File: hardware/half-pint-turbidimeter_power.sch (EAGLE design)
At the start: 17 parts, among them U1 MCP73831

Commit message: minor edits to eagle schematics
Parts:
- removed D11: RED, SparkFun:LED0603
- removed JP2: STAND-OFF, SparkFun:STAND-OFF
- removed R2K: 2K, SparkFun:RESISTOR0402-RES
- removed R330: 330, SparkFun:RESISTOR0402-RES
- added D2: GREEN, SparkFun:LED0603
- added FRAME1: FRAME-LETTER, SparkFun-Aesthetics:FRAME-LETTER
- added R2: R330, SparkFun:RESISTOR0402-RES
- added R3: R2K, SparkFun:RESISTOR0402-RES
- D1: value GREEN -> RED
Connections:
- net GND: now also D2.C, R3.2; no longer D1.C, R2K.2
- net N$2: now also D2.A, R2.2; no longer D1.A, R1.2
- net N$3: now also D1.A, R1.1; no longer D11.A, R330.1
- net PROG: now also R3.1; no longer R2K.1
- net STAT: now also D1.C, R2.1; no longer D11.C, R1.1
- net VIN: now also R1.2; no longer R330.2
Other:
- note added: "AWQUA"
- note removed: "0.1""
- note removed: "Connection to 3.7V System"
- note removed: "N. Seidle"
- note removed: "Set for 500mA charging"
- moved on the sheet: +OUT-, 1UF, 2.2UF, D1, OPT_10NF, R1

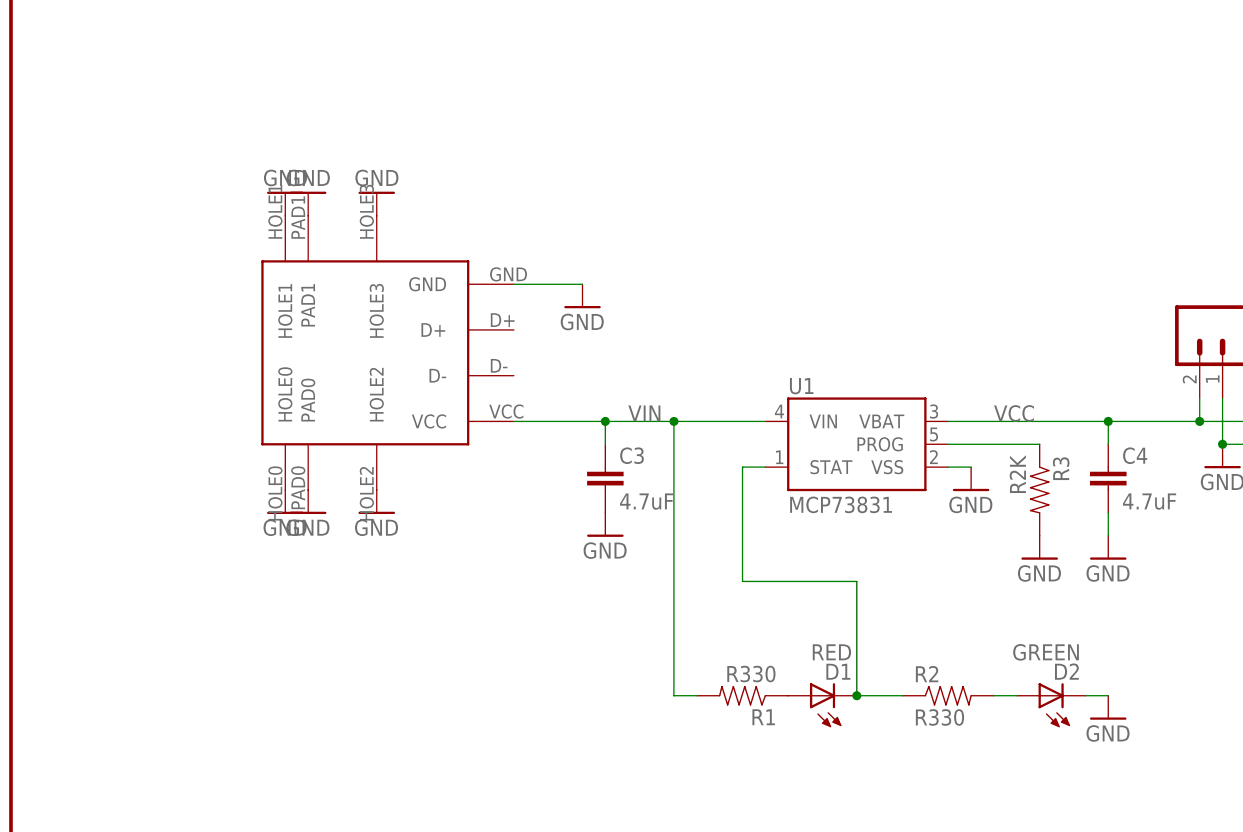
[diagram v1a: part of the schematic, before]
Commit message: added voltage protection diode
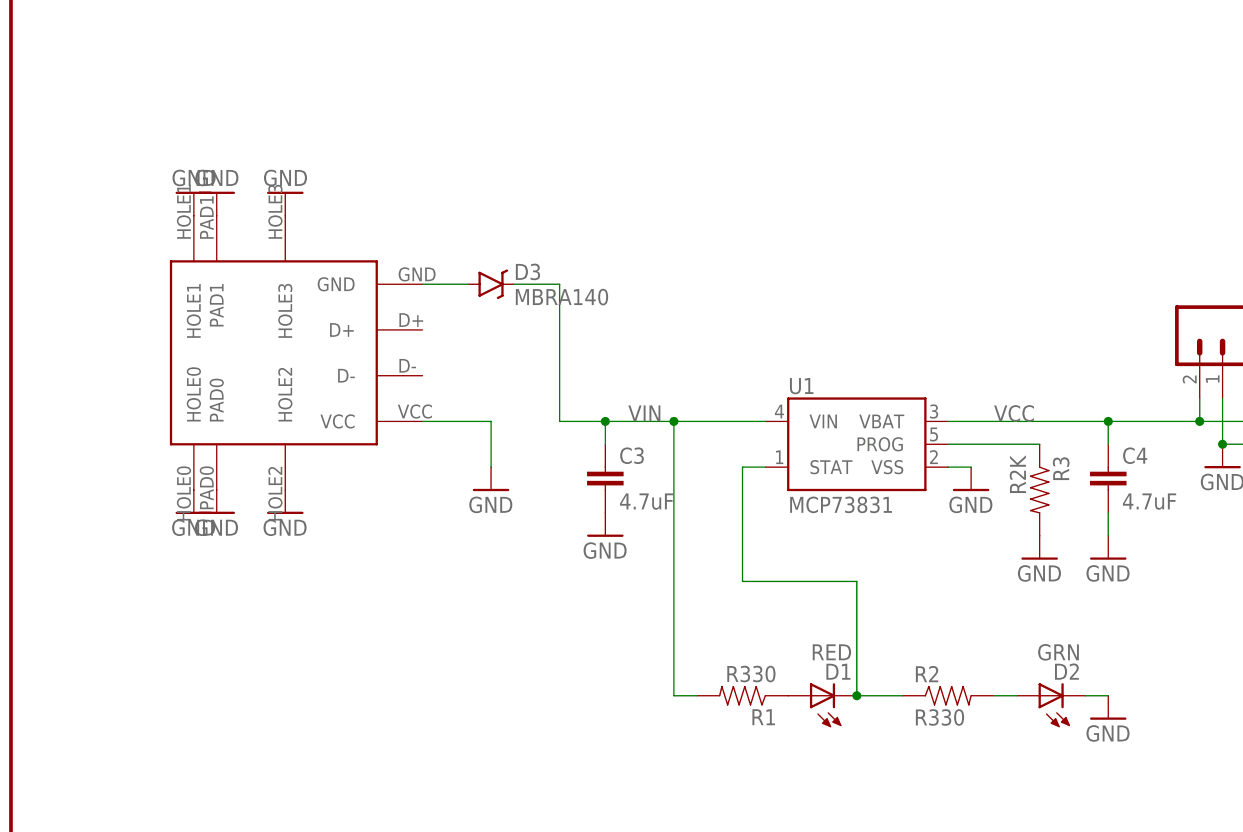
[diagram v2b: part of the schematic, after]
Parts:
- added D3: MBRA140, SparkFun-DiscreteSemi:MBRA140
- D2: value GREEN -> GRN
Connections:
- new net N$5: D3.A, U$3.GND
- net GND: now also U$3.VCC; no longer U$3.GND
- net VIN: now also D3.C; no longer U$3.VCC
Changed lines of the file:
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@@
 <part name="2.2UF" library="SparkFun-Passives" deviceset="CAP" device="0603-CAP"/>
 <part name="R2" library="SparkFun" deviceset="RESISTOR" device="0402-RES" value="R330"/>
-<part name="D2" library="SparkFun" deviceset="LED" device="0603" value="GREEN"/>
+<part name="D2" library="SparkFun" deviceset="LED" device="0603" value="GRN"/>
 <part name="GND3" library="SparkFun" deviceset="GND" device=""/>
 <part name="U$3" library="awqua_eagle_library" deviceset="USBMICRO-DX4R005JJ2" device=""/>
@@
 <part name="GND9" library="SparkFun" deviceset="GND" device=""/>
 <part name="FRAME1" library="SparkFun-Aesthetics" deviceset="FRAME-LETTER" device=""/>
+<part name="D3" library="SparkFun-DiscreteSemi" deviceset="MBRA140" device=""/>
 </parts>
 <sheets>
@@
 <instance part="D1" gate="G$1" x="111.76" y="88.9" rot="R90"/>
 <instance part="R1" gate="G$1" x="104.14" y="88.9" rot="R180"/>
-<instance part="GND15" gate="1" x="86.36" y="132.08"/>
+<instance part="GND15" gate="1" x="76.2" y="111.76"/>
 <instance part="GND14" gate="1" x="144.78" y="104.14"/>
 <instance part="GND17" gate="1" x="88.9" y="106.68"/>
@@
 <instance part="D2" gate="G$1" x="137.16" y="88.9" rot="R90"/>
 <instance part="GND3" gate="1" x="144.78" y="86.36"/>
-<instance part="U$3" gate="G$1" x="50.8" y="114.3"/>
-<instance part="GND4" gate="1" x="53.34" y="144.78" rot="R180"/>
-<instance part="GND5" gate="1" x="55.88" y="144.78" rot="R180"/>
-<instance part="GND6" gate="1" x="63.5" y="144.78" rot="R180"/>
-<instance part="GND7" gate="1" x="63.5" y="109.22"/>
-<instance part="GND8" gate="1" x="55.88" y="109.22"/>
-<instance part="GND9" gate="1" x="53.34" y="109.22"/>
+<instance part="U$3" gate="G$1" x="40.64" y="114.3"/>
+<instance part="GND4" gate="1" x="43.18" y="144.78" rot="R180"/>
+<instance part="GND5" gate="1" x="45.72" y="144.78" rot="R180"/>
+<instance part="GND6" gate="1" x="53.34" y="144.78" rot="R180"/>
+<instance part="GND7" gate="1" x="53.34" y="109.22"/>
+<instance part="GND8" gate="1" x="45.72" y="109.22"/>
+<instance part="GND9" gate="1" x="43.18" y="109.22"/>
 <instance part="FRAME1" gate="G$1" x="22.86" y="30.48"/>
 <instance part="FRAME1" gate="V" x="170.18" y="30.48"/>
+<instance part="D3" gate="G$1" x="76.2" y="134.62"/>
 </instances>
 <busses>
@@
 <segment>
 <pinref part="GND15" gate="1" pin="GND"/>
-<pinref part="U$3" gate="G$1" pin="GND"/>
-<wire x1="86.36" y1="134.62" x2="78.74" y2="134.62" width="0.1524" layer="91"/>
+<wire x1="76.2" y1="114.3" x2="76.2" y2="119.38" width="0.1524" layer="91"/>
+<wire x1="68.58" y1="119.38" x2="76.2" y2="119.38" width="0.1524" layer="91"/>
+<pinref part="U$3" gate="G$1" pin="VCC"/>
 </segment>
 <segment>
@@
 </segment>
 </net>
+<net name="N$1" class="0">
+<segment>
+<pinref part="U$2" gate="G$1" pin="BYP"/>
+<pinref part="OPT_10NF" gate="G$1" pin="1"/>
+<wire x1="241.3" y1="86.36" x2="241.3" y2="88.9" width="0.1524" layer="91"/>
+</segment>
+</net>
+<net name="N$4" class="0">
+<segment>
+<pinref part="U$2" gate="G$1" pin="VOUT"/>
+<pinref part="2.2UF" gate="G$1" pin="1"/>
+<wire x1="248.92" y1="93.98" x2="241.3" y2="93.98" width="0.1524" layer="91"/>
+<pinref part="+OUT-" gate="G$1" pin="1"/>
+<wire x1="248.92" y1="93.98" x2="248.92" y2="99.06" width="0.1524" layer="91"/>
+<junction x="248.92" y="93.98"/>
+</segment>
+</net>
+<net name="N$2" class="0">
+<segment>
+<pinref part="R2" gate="G$1" pin="2"/>
+<pinref part="D2" gate="G$1" pin="A"/>
+<wire x1="134.62" y1="88.9" x2="132.08" y2="88.9" width="0.1524" layer="91"/>
+</segment>
+</net>
+<net name="N$5" class="0">
+<segment>
+<pinref part="D3" gate="G$1" pin="A"/>
+<pinref part="U$3" gate="G$1" pin="GND"/>
+<wire x1="68.58" y1="134.62" x2="73.66" y2="134.62" width="0.1524" layer="91"/>
+</segment>
+</net>
 <net name="VIN" class="0">
 <segment>
@@
 <wire x1="99.06" y1="88.9" x2="96.52" y2="88.9" width="0.1524" layer="91"/>
 <wire x1="96.52" y1="88.9" x2="96.52" y2="119.38" width="0.1524" layer="91"/>
-<wire x1="78.74" y1="119.38" x2="88.9" y2="119.38" width="0.1524" layer="91"/>
 <junction x="88.9" y="119.38"/>
 <junction x="96.52" y="119.38"/>
@@
 <pinref part="U1" gate="G$1" pin="VIN"/>
 <pinref part="C3" gate="G$1" pin="1"/>
-<pinref part="U$3" gate="G$1" pin="VCC"/>
-</segment>
-</net>
-<net name="N$1" class="0">
-<segment>
-<pinref part="U$2" gate="G$1" pin="BYP"/>
-<pinref part="OPT_10NF" gate="G$1" pin="1"/>
-<wire x1="241.3" y1="86.36" x2="241.3" y2="88.9" width="0.1524" layer="91"/>
-</segment>
-</net>
-<net name="N$4" class="0">
-<segment>
-<pinref part="U$2" gate="G$1" pin="VOUT"/>
-<pinref part="2.2UF" gate="G$1" pin="1"/>
-<wire x1="248.92" y1="93.98" x2="241.3" y2="93.98" width="0.1524" layer="91"/>
-<pinref part="+OUT-" gate="G$1" pin="1"/>
-<wire x1="248.92" y1="93.98" x2="248.92" y2="99.06" width="0.1524" layer="91"/>
-<junction x="248.92" y="93.98"/>
-</segment>
-</net>
-<net name="N$2" class="0">
-<segment>
-<pinref part="R2" gate="G$1" pin="2"/>
-<pinref part="D2" gate="G$1" pin="A"/>
-<wire x1="134.62" y1="88.9" x2="132.08" y2="88.9" width="0.1524" layer="91"/>
-</segment>
-</net>
+<wire x1="83.82" y1="119.38" x2="88.9" y2="119.38" width="0.1524" layer="91"/>
+<wire x1="83.82" y1="119.38" x2="83.82" y2="134.62" width="0.1524" layer="91"/>
+<pinref part="D3" gate="G$1" pin="C"/>
+<wire x1="78.74" y1="134.62" x2="83.82" y2="134.62" width="0.1524" layer="91"/>
+</segment>
+</net>
